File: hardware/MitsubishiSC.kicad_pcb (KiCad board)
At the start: 6 copper layers, 30 x 50 mm, 68 parts, among them J1 CN105, J2 USB_C_Receptacle_USB2.0_16P, Q1 BSS138, Q2 BSS138, SW3 SPST, SW4 SPST, U1 TPS562203, U3 ESP32-C3-WROOM-02, U4 USBLC6-2SC6, U5 TLV75733PDBV

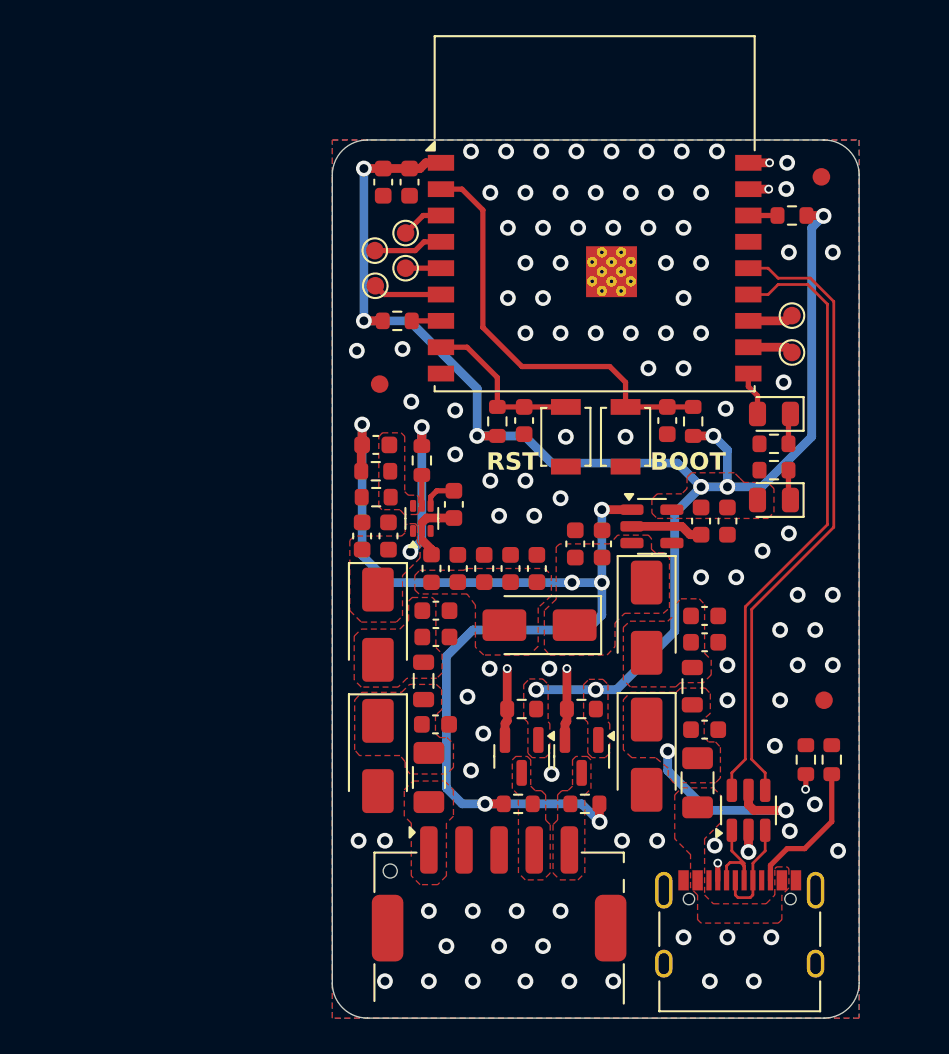
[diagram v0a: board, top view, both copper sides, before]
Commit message: feat(pcb): revamp design and layout
This commit makes significant changes to the PCB, primarily changing the
MCU from ESP32-C3 to ESP32-C6 to accommodate Matter-over-Thread.
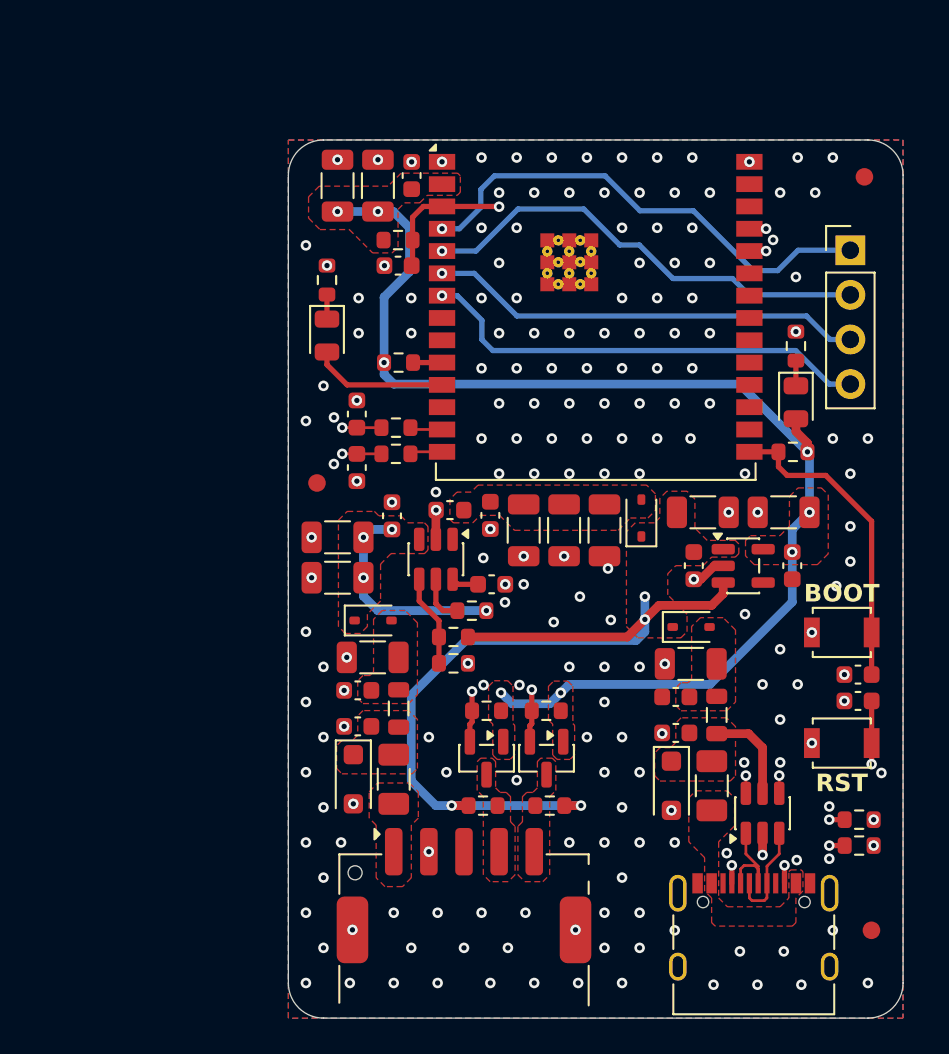
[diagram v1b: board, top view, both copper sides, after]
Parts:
- removed TP1, TP2, TP3, TP4, TP5, TP6: TestPoint, TestPoint:TestPoint_Pad_D1.0mm
- added C23: 100nF, Capacitor_SMD:C_0603_1608Metric, F.Cu at (149.5, 81.6)
- added C24: NC, Capacitor_SMD:C_0603_1608Metric, F.Cu at (146.4, 98.2)
- added C25: NC, Capacitor_SMD:C_0603_1608Metric, F.Cu at (146.4, 95.2)
- added C26: 100nF, Capacitor_SMD:C_0603_1608Metric, F.Cu at (148.7, 86.8)
- added J3: Conn_01x04, Connector_PinHeader_2.54mm:PinHeader_1x04_P2.54mm_Vertical, F.Cu at (174.5, 85.9)
- added R16: 22R, Resistor_SMD:R_0603_1608Metric, F.Cu at (148.6, 97.5)
- C1, C16, C17, C20, C22: footprint Capacitor_SMD:C_0603_1608Metric -> Capacitor_SMD:C_1206_3216Metric
- C10, C11, C21, C7: value 4.7uF -> 10uF; footprint Capacitor_SMD:C_0603_1608Metric -> Capacitor_SMD:C_1206_3216Metric
- C12: value 100nF -> 10uF; footprint Capacitor_SMD:C_0603_1608Metric -> Capacitor_SMD:C_1206_3216Metric
- C5: value 47pF -> 10uF; footprint Capacitor_SMD:C_0603_1608Metric -> Capacitor_SMD:C_1206_3216Metric
- D1: value SMAJ12A -> SMF4L12A; footprint Diode_SMD:D_SMA -> Diode_SMD:D_SOD-123F
- D2, D4, D7: value SS14 -> CUS10S30; footprint Diode_SMD:D_SMA -> Diode_SMD:D_SOD-323
- D8: value SMAJ5.0A -> SMF4L5.0A; footprint Diode_SMD:D_SMA -> Diode_SMD:D_SOD-123F
- L1: value 4.7uH -> 3.3uH
- R10: value 220kR -> 54.9kR
- R11: value 30kR -> 10kR
- R5: value 100kR -> 10kR
- R7: value 10kR -> 22R
- U1: value TPS562203 -> TPS563201; footprint Package_TO_SOT_SMD:SOT-563 -> Package_TO_SOT_SMD:SOT-23-6
- U3: value ESP32-C3-WROOM-02 -> ESP32-C6-WROOM-1; footprint RF_Module:ESP32-C3-WROOM-02 -> _Custom:ESP32-C6-WROOM-1
- moved R8 27.1 mm to (144.7, 87.6), turned to 90 degrees
- moved D5 25.8 mm to (144.7, 90.7), turned to -90 degrees
- moved R7 25.6 mm to (148.6, 96.0), turned to 0 degrees
- moved C19 24.8 mm to (174.9, 111.5), turned to 180 degrees
- moved SW4 23.5 mm to (174.0, 113.9), turned to 180 degrees
- moved C18 18.1 mm to (174.9, 110.0), turned to 180 degrees
- moved SW3 16.6 mm to (174.0, 107.6), turned to 180 degrees
- moved FID2 13.4 mm to (175.7, 124.6)
- moved R13 11.8 mm to (148.7, 85.3), turned to 0 degrees
- moved R11 10.4 mm to (151.9, 109.4), turned to 0 degrees
- moved R10 10.4 mm to (151.9, 107.9), turned to 180 degrees
- moved R5 9.01 mm to (152.9, 106.4), turned to 180 degrees
- moved D2 8.42 mm to (162.6, 101.1), turned to 90 degrees
- moved C5 7.87 mm to (145.3, 104.5), turned to 180 degrees
- moved C7 7.48 mm to (166.1, 100.8), turned to 0 degrees
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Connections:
- C18 pad 1: /ESP32_BOOT -> /MCU_BOOT
- C19 pad 1: /ESP32_RESET -> /MCU_RST
- C5 pad 1: +5V -> +12V
- C5 pad 2: /SMPS_FB -> GND
- D5 pad 2: /ESP32_LED_STAT -> /MCU_LED_STAT
- Q1 pad 2: /ESP32_UART1_RX -> /MCU_UART_RX
- Q2 pad 2: /ESP32_UART1_TX -> /MCU_UART_TX
- R1 pad 2: /ESP32_UART1_RX -> /MCU_UART_RX
- R12 pad 2: /ESP32_GPIO8 -> /MCU_GPIO8
- R13 pad 2: /ESP32_RESET -> /MCU_RST
- R4 pad 2: /ESP32_UART1_TX -> /MCU_UART_TX
- R6 pad 2: /ESP32_BOOT -> /MCU_BOOT
- R7 pad 1: +3.3V -> /ESD_USB_D-
- R7 pad 2: /ESP32_GPIO2 -> /MCU_USB_D-
- SW3 pad 1: /ESP32_BOOT -> /MCU_BOOT
- SW4 pad 1: /ESP32_RESET -> /MCU_RST
- U1 pad 1: +12V -> GND
- U1 pad 3: GND -> +12V
- U1 pad 4: /SMPS_BST -> /SMPS_FB
- U1 pad 6: /SMPS_FB -> /SMPS_BST
- U3 pad 1: +3.3V -> GND
- U3 pad 10: /ESP32_LED_STAT -> /MCU_GPIO8
- U3 pad 11: /ESP32_UART0_RX -> /MCU_LED_STAT
- U3 pad 12: /ESP32_UART0_TX -> unconnected-(U3-IO11-Pad12)
- U3 pad 13: /ESP32_USB_D- -> /MCU_USB_D-
- U3 pad 14: /ESP32_USB_D+ -> /MCU_USB_D+
- U3 pad 15: unconnected-(U3-IO3-Pad15) -> /MCU_BOOT
- U3 pad 16: /ESP32_GPIO2 -> unconnected-(U3-IO18-Pad16)
- U3 pad 17: /ESP32_UART1_TX -> unconnected-(U3-IO19-Pad17)
- U3 pad 18: /ESP32_UART1_RX -> unconnected-(U3-IO20-Pad18)
- U3 pad 19: GND -> unconnected-(U3-IO21-Pad19)
- U3 pad 2: /ESP32_BOOT -> +3.3V
- U3 pad 3: /ESP32_JTAG_TMS -> /MCU_RST
- U3 pad 4: /ESP32_JTAG_TDI -> /MCU_GPIO4
- U3 pad 5: /ESP32_JTAG_TCK -> /MCU_GPIO5
- U3 pad 6: /ESP32_JTAG_TDO -> /MCU_GPIO6
- U3 pad 7: /ESP32_GPIO8 -> /MCU_GPIO7
- U3 pad 8: /ESP32_RESET -> unconnected-(U3-IO0-Pad8)
- U3 pad 9: GND -> unconnected-(U3-IO1-Pad9)
- U4 pad 4: /ESP32_USB_D+ -> /ESD_USB_D+
- U4 pad 6: /ESP32_USB_D- -> /ESD_USB_D-
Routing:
- net /MCU_RST: track 0.00 -> 65.0 mm, vias 0 -> 2
- net /ESD_USB_D-: track 0.00 -> 44.3 mm, vias 0 -> 2
- net /ESD_USB_D+: track 0.00 -> 43.7 mm, vias 0 -> 2
- net /ESP32_UART1_RX: track 43.5 -> 0.00 mm, vias 2 -> 0
- net /ESP32_UART1_TX: track 38.7 -> 0.00 mm, vias 2 -> 0
- net /MCU_UART_TX: track 0.00 -> 38.5 mm, vias 0 -> 2
- net /MCU_UART_RX: track 0.00 -> 37.0 mm, vias 0 -> 2
- net /ESP32_USB_D+: track 35.7 -> 0.00 mm
- net /ESP32_USB_D-: track 35.1 -> 0.00 mm
- net /MCU_GPIO4: track 0.00 -> 27.8 mm, vias 0 -> 1
- net /MCU_GPIO5: track 0.00 -> 26.3 mm, vias 0 -> 1
- net /MCU_GPIO7: track 0.00 -> 26.0 mm, vias 0 -> 1
- net /MCU_GPIO6: track 0.00 -> 24.8 mm, vias 0 -> 1
- net /ESP32_BOOT: track 24.2 -> 0.00 mm
- net /MCU_BOOT: track 0.00 -> 17.8 mm
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- removed copper zone on F.Cu, net /SMPS_FB
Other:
- board size 30 x 50 mm -> 35 x 50 mm
- board text added: "Matter Controller for"
- board text removed: "HomeKit Controller for"

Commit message: feat: redesign PCB layout (#41)
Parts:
- removed C22: 10uF, Capacitor_SMD:C_1206_3216Metric
- removed C23, C26: 100nF, Capacitor_SMD:C_0603_1608Metric
- removed C24, C25: NC, Capacitor_SMD:C_0603_1608Metric
- removed D7: CUS10S30, Diode_SMD:D_SOD-323
- removed D8: SMF4L5.0A, Diode_SMD:D_SOD-123F
- removed FB2: 220R@100MHz, Inductor_SMD:L_0805_2012Metric
- removed J3: Conn_01x04, Connector_PinHeader_2.54mm:PinHeader_1x04_P2.54mm_Vertical
- removed SW3, SW4: SPST, Button_Switch_SMD:SW_SPST_B3U-1000P
- removed U5: TLV75733PDBV, Package_TO_SOT_SMD:SOT-23-5
- added D6: BU, LED_SMD:LED_0805_2012Metric, F.Cu at (171.1, 104.5)
- added H1: #2, MountingHole:MountingHole_2.5mm_Pad_Via, F.Cu at (168.1, 83.1)
- added H2: #2, MountingHole:MountingHole_2.5mm_Pad_Via, F.Cu at (138.1, 113.1)
- added R17: 10kR, Resistor_SMD:R_0603_1608Metric, F.Cu at (157.8, 106.0)
- added R18: 10kR, Resistor_SMD:R_0603_1608Metric, F.Cu at (158.1, 100.6)
- added R19: 10kR, Resistor_SMD:R_0603_1608Metric, F.Cu at (171.1, 108.5)
- added R20: 10kR, Resistor_SMD:R_0603_1608Metric, F.Cu at (171.1, 102.7)
- added SW1: SPST, Button_Switch_SMD:SW_SPST_PTS810, F.Cu at (171.7, 92.7)
- added SW2: SPST, Button_Switch_SMD:SW_SPST_PTS810, F.Cu at (171.7, 96.5)
- added U2: TPS54202DDC, Package_TO_SOT_SMD:SOT-23-6, F.Cu at (136.5, 99.8)
- C11, C17, C20, C21: value 10uF -> 100nF; footprint Capacitor_SMD:C_1206_3216Metric -> Capacitor_SMD:C_0603_1608Metric
- C13, C14, C15, C19: value 100nF -> 10uF; footprint Capacitor_SMD:C_0603_1608Metric -> Capacitor_SMD:C_1206_3216Metric
- C16: value 10uF -> 68pF; footprint Capacitor_SMD:C_1206_3216Metric -> Capacitor_SMD:C_0603_1608Metric
- D1: value SMF4L12A -> CUS10S30; footprint Diode_SMD:D_SOD-123F -> Diode_SMD:D_SOD-323
- D3: value RED -> SMF4L12A; footprint LED_SMD:LED_0805_2012Metric -> Diode_SMD:D_SOD-123F
- D4: value CUS10S30 -> SMF4L5.0A; footprint Diode_SMD:D_SOD-323 -> Diode_SMD:D_SOD-123F
- D5: value BLUE -> RD
- F2: value 350mA -> 125mA
- J2: value USB_C_Receptacle_USB2.0_16P -> TC2050; footprint Connector_USB:USB_C_Receptacle_XKB_U262-16XN-4BVC11 -> Connector:Tag-Connect_TC2050-IDC-NL_2x05_P1.27mm_Vertical
- L1: value 3.3uH -> 15uH; footprint Inductor_SMD:L_0603_1608Metric -> Inductor_SMD:L_TDK_VLS6045EX_VLS6045AF
- R10: value 54.9kR -> 10kR
- R11, R12, R3, R4, R6: value 10kR -> 0R
- R13: value 10kR -> 100kR
- R14: value 5.1kR -> 13.3kR
- R15: value 5.1kR -> 10kR
- R16: value 22R -> 10kR
- R5: value 10kR -> 470R
- R7: value 22R -> 0R
- R9: value 1kR -> 0R
- U1: value TPS563201 -> ESP32-C6-WROOM-1; footprint Package_TO_SOT_SMD:SOT-23-6 -> _Custom:ESP32-C6-WROOM-1
- U3: value ESP32-C6-WROOM-1 -> TLV75733PDBV; footprint _Custom:ESP32-C6-WROOM-1 -> Package_TO_SOT_SMD:SOT-23-5
- moved FID3 48.9 mm to (141.1, 116.6)
- moved R14 43.2 mm to (138.3, 97.0)
- moved FID2 38.3 mm to (171.1, 86.6)
- moved C14 36.2 mm to (132.4, 94.6), turned to 0 degrees
- moved R3 35.7 mm to (140.3, 86.1), turned to 0 degrees
- moved C19 34.4 mm to (140.7, 108.4), turned to -90 degrees
- moved C4 33.7 mm to (135.6, 96.3), turned to 90 degrees
- moved C18 32.3 mm to (142.6, 109.7), turned to -90 degrees
- moved R1 31.4 mm to (141.1, 83.4), turned to -90 degrees
- moved R9 31.1 mm to (140.3, 90.6), turned to 0 degrees
- moved D5 30.9 mm to (171.1, 106.8), turned to 180 degrees
- moved FID1 30.1 mm to (171.1, 112.6)
- moved R4 29.7 mm to (140.3, 87.6)
- moved D1 29.3 mm to (132.4, 90.2), turned to 180 degrees
- moved D3 28.8 mm to (146.5, 109.0)
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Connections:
- C1 pad 1: +12V -> +3.3V
- C11 pad 1: +3.3V -> /SMPS_SW_5V
- C12 pad 1: +3.3V -> /SMPS_SW_5V
- C13 pad 1: /CN105_12V_FLT -> /SMPS_SW_5V
- C14 pad 1: /USB_5V_D -> /SMPS_SW_5V
- C15 pad 1: /CN105_12V_D -> /SMPS_SW_5V
- C16 pad 1: /SMPS_5V_D -> +5V
- C16 pad 2: GND -> /SMPS_FB
- C17 pad 1: /SMPS_5V_D -> /CN105_12V_FSD
- C18 pad 1: /MCU_BOOT -> /CN105_12V_FLT
- C19 pad 1: /MCU_RST -> /CN105_12V_FLT
- C2 pad 1: /SMPS_5V -> +3.3V
- C2 pad 2: /SMPS_BST -> GND
- C20 pad 1: /CN105_12V_D -> /MCU_RST
- C21 pad 1: /USB_5V_D -> /MCU_BOOT
- C3 pad 1: +12V -> /MCU_RST
- C4 pad 1: /USB_5V_FLT -> /SMPS_BOOT
- C4 pad 2: GND -> /SMPS_SW
- C6 pad 1: /SMPS_5V_D -> +12V
- D1 pad 1: /CN105_12V_FLT -> +5V
- D1 pad 2: GND -> /SMPS_SW_5V
- D2 pad 1: +5V -> +12V
- D2 pad 2: /SMPS_5V_D -> /CN105_12V_FLT
- D3 pad 1: Net-(D3-K) -> /CN105_12V_FSD
- D3 pad 2: +3.3V -> GND
- D4 pad 1: +5V -> /CN105_5V_FSD
- D4 pad 2: /USB_5V_D -> GND
- D5 pad 1: Net-(D5-K) -> /MCU_3V3_K
- D5 pad 2: /MCU_LED_STAT -> +3.3V
- F1 pad 2: /CN105_12V_FLT -> /CN105_12V_FSD
- F2 pad 1: /USB_5V -> /CN105_5V
- F2 pad 2: /USB_5V_FLT -> /CN105_5V_FSD
- FB1 pad 1: /USB_5V_FLT -> /CN105_12V_FSD
- FB1 pad 2: /USB_5V_D -> /CN105_12V_FLT
- J1 pad 3: unconnected-(J1-5V-Pad3) -> /CN105_5V
- L1 pad 1: /SMPS_5V -> /SMPS_SW
- L1 pad 2: /SMPS_5V_D -> /SMPS_SW_5V
- Q1 pad 2: /MCU_UART_RX -> /CN105_TXL
- Q1 pad 3: /CN105_TX -> /CN105_TXH
- Q2 pad 2: /MCU_UART_TX -> /CN105_RXL
- Q2 pad 3: /CN105_RX -> /CN105_RXH
- R1 pad 2: /MCU_UART_RX -> /MCU_RST
- R10 pad 1: +5V -> +3.3V
- R10 pad 2: /SMPS_FB -> /MCU_IO08
- R11 pad 1: /SMPS_FB -> /DBG_TXD
- R11 pad 2: GND -> /MCU_RX0
- R12 pad 1: +3.3V -> /MCU_TX0
- R12 pad 2: /MCU_GPIO8 -> /DBG_RXD
- R13 pad 1: +3.3V -> +5V
- R13 pad 2: /MCU_RST -> /SMPS_FB
- R14 pad 1: /USB_CC2 -> /SMPS_FB
- R15 pad 1: /USB_CC1 -> /CN105_5V_FSD
- R15 pad 2: GND -> /CN105_TXH
- R16 pad 1: /MCU_USB_D+ -> +3.3V
- R16 pad 2: /ESD_USB_D+ -> /CN105_TXL
- R2 pad 1: +5V -> +3.3V
- R2 pad 2: /CN105_TX -> /MCU_BOOT
- R3 pad 1: +5V -> /DBG_JTMS
- R3 pad 2: /CN105_RX -> /MCU_MTMS
- R4 pad 1: +3.3V -> /MCU_MTDI
- R4 pad 2: /MCU_UART_TX -> /DBG_JTDI
- R5 pad 1: +12V -> /CN105_RXL
- R5 pad 2: /SMPS_EN -> /MCU_TX1
- R6 pad 1: +3.3V -> /MCU_RX1
- R6 pad 2: /MCU_BOOT -> /CN105_TXL
- R7 pad 1: /ESD_USB_D- -> /MCU_MTCK
- R7 pad 2: /MCU_USB_D- -> /DBG_JTCK
- R8 pad 1: Net-(D5-K) -> /MCU_IO15
- R9 pad 1: Net-(D3-K) -> /DBG_JTDO
- R9 pad 2: GND -> /MCU_MTDO
- U1 pad 2: /SMPS_5V -> +3.3V
- U1 pad 3: +12V -> /MCU_RST
- U1 pad 4: /SMPS_FB -> /MCU_MTMS
- U1 pad 5: /SMPS_EN -> /MCU_MTDI
- U1 pad 6: /SMPS_BST -> /MCU_MTCK
- U3 pad 1: GND -> +5V
- U3 pad 2: +3.3V -> GND
- U3 pad 3: /MCU_RST -> +5V
- U3 pad 4: /MCU_GPIO4 -> unconnected-(U3-NC-Pad4)
- U3 pad 5: /MCU_GPIO5 -> +3.3V
- U4 pad 1: /USB_D- -> /CN105_TX
- U4 pad 3: /USB_D+ -> /CN105_RX
- U4 pad 4: /ESD_USB_D+ -> /CN105_RXH
- U4 pad 5: /USB_5V_FLT -> /CN105_5V_FSD
- U4 pad 6: /ESD_USB_D- -> /CN105_TXH
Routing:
- net /ESD_USB_D-: track 44.3 -> 0.00 mm, vias 2 -> 0
- net /ESD_USB_D+: track 43.7 -> 0.00 mm, vias 2 -> 0
- net /DBG_JTMS: track 0.00 -> 39.1 mm, vias 0 -> 2
- net /MCU_UART_TX: track 38.5 -> 0.00 mm, vias 2 -> 0
- net /MCU_UART_RX: track 37.0 -> 0.00 mm, vias 2 -> 0
- net /DBG_JTCK: track 0.00 -> 31.5 mm, vias 0 -> 2
- net /DBG_JTDO: track 0.00 -> 31.1 mm, vias 0 -> 2
- net /DBG_JTDI: track 0.00 -> 30.9 mm, vias 0 -> 2
- net +5V: track 50.0 -> 20.1 mm, vias 4 -> 5
- net /MCU_GPIO4: track 27.8 -> 0.00 mm, vias 1 -> 0
- net /MCU_GPIO5: track 26.3 -> 0.00 mm, vias 1 -> 0
- net /MCU_GPIO7: track 26.0 -> 0.00 mm, vias 1 -> 0
- net /MCU_GPIO6: track 24.8 -> 0.00 mm, vias 1 -> 0
- net /DBG_TXD: track 0.00 -> 24.6 mm, vias 0 -> 2
- net /DBG_RXD: track 0.00 -> 22.4 mm, vias 0 -> 2
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- added copper zone on F.Cu, net /CN105_12V_FSD
- added copper zone on F.Cu, net /CN105_5V
- added copper zone on F.Cu, net /CN105_5V_FSD
- added copper zone on F.Cu, net /SMPS_FB
- added copper zone on F.Cu, net /SMPS_SW_5V
- removed copper zone on F.Cu, net /CN105_12V_D
- removed copper zone on F.Cu, net /CN105_RX
- removed copper zone on F.Cu, net /CN105_TX
- removed copper zone on F.Cu, net /SMPS_5V_D
- removed copper zone on F.Cu, net /USB_5V
- removed copper zone on F.Cu, net /USB_5V_D
- removed copper zone on F.Cu, net /USB_5V_FLT
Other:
- board size 35 x 50 mm -> 50 x 43 mm
- board text added: "RESET"
- board text removed: "RST"
